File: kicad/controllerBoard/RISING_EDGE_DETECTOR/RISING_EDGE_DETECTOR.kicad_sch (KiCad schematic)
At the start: 17 parts, among them Q385 Q_PMOS_GSD, Q386 Q_NMOS_GSD, Q387 Q_PMOS_GSD, Q388 Q_NMOS_GSD, Q389 Q_PMOS_GSD, Q390 Q_NMOS_GSD, Q391 Q_PMOS_GSD, Q392 Q_NMOS_GSD

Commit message: add mounting holes
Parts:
- renumbered C3 to C1, C4 to C2, C5 to C3
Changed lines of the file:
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@@
 		(dnp no)
 		(fields_autoplaced yes)
-		(property "Reference" "#PWR090"
+		(property "Reference" "#PWR0138"
 			(at 120.65 80.01 0)
 			(hide yes)
@@
 			(project "controllerBoard"
 				(path "/93a9a1ca-4ee5-40da-ab67-92836146c003/96d1d3a9-3ebd-46ac-a2d2-b692fac1af2c"
-					(reference "#PWR090")
+					(reference "#PWR0138")
 					(unit 1)
 				)
 				(path "/93a9a1ca-4ee5-40da-ab67-92836146c003/def1fdf8-7002-45c6-87e0-28926b899265"
-					(reference "#PWR0122")
+					(reference "#PWR0204")
 					(unit 1)
 				)
@@
 		(dnp no)
 		(fields_autoplaced yes)
-		(property "Reference" "#PWR093"
+		(property "Reference" "#PWR0141"
 			(at 173.99 86.36 0)
 			(hide yes)
@@
 			(project "controllerBoard"
 				(path "/93a9a1ca-4ee5-40da-ab67-92836146c003/96d1d3a9-3ebd-46ac-a2d2-b692fac1af2c"
-					(reference "#PWR093")
+					(reference "#PWR0141")
 					(unit 1)
 				)
 				(path "/93a9a1ca-4ee5-40da-ab67-92836146c003/def1fdf8-7002-45c6-87e0-28926b899265"
-					(reference "#PWR0125")
+					(reference "#PWR0207")
 					(unit 1)
 				)
@@
 		(dnp no)
 		(fields_autoplaced yes)
-		(property "Reference" "#PWR088"
+		(property "Reference" "#PWR0136"
 			(at 99.06 52.07 0)
 			(hide yes)
@@
 			(project "controllerBoard"
 				(path "/93a9a1ca-4ee5-40da-ab67-92836146c003/96d1d3a9-3ebd-46ac-a2d2-b692fac1af2c"
-					(reference "#PWR088")
+					(reference "#PWR0136")
 					(unit 1)
 				)
 				(path "/93a9a1ca-4ee5-40da-ab67-92836146c003/def1fdf8-7002-45c6-87e0-28926b899265"
-					(reference "#PWR0120")
+					(reference "#PWR0202")
 					(unit 1)
 				)
@@
 		(dnp no)
 		(fields_autoplaced yes)
-		(property "Reference" "#PWR092"
+		(property "Reference" "#PWR0140"
 			(at 157.48 82.55 0)
 			(hide yes)
@@
 			(project "controllerBoard"
 				(path "/93a9a1ca-4ee5-40da-ab67-92836146c003/96d1d3a9-3ebd-46ac-a2d2-b692fac1af2c"
-					(reference "#PWR092")
+					(reference "#PWR0140")
 					(unit 1)
 				)
 				(path "/93a9a1ca-4ee5-40da-ab67-92836146c003/def1fdf8-7002-45c6-87e0-28926b899265"
-					(reference "#PWR0124")
+					(reference "#PWR0206")
 					(unit 1)
 				)
@@
 		(dnp no)
 		(fields_autoplaced yes)
-		(property "Reference" "#PWR094"
+		(property "Reference" "#PWR0142"
 			(at 201.93 62.23 0)
 			(hide yes)
@@
 			(project "controllerBoard"
 				(path "/93a9a1ca-4ee5-40da-ab67-92836146c003/96d1d3a9-3ebd-46ac-a2d2-b692fac1af2c"
-					(reference "#PWR094")
+					(reference "#PWR0142")
 					(unit 1)
 				)
 				(path "/93a9a1ca-4ee5-40da-ab67-92836146c003/def1fdf8-7002-45c6-87e0-28926b899265"
-					(reference "#PWR0126")
+					(reference "#PWR0208")
 					(unit 1)
 				)
@@
 		(dnp no)
 		(fields_autoplaced yes)
-		(property "Reference" "C3"
+		(property "Reference" "C1"
 			(at 107.95 58.42 90)
 			(show_name no)
@@
 			(project "controllerBoard"
 				(path "/93a9a1ca-4ee5-40da-ab67-92836146c003/96d1d3a9-3ebd-46ac-a2d2-b692fac1af2c"
-					(reference "C3")
+					(reference "C1")
 					(unit 1)
 				)
 				(path "/93a9a1ca-4ee5-40da-ab67-92836146c003/def1fdf8-7002-45c6-87e0-28926b899265"
-					(reference "C14")
+					(reference "C12")
 					(unit 1)
 				)
@@
 		(dnp no)
 		(fields_autoplaced yes)
-		(property "Reference" "C4"
+		(property "Reference" "C2"
 			(at 198.12 50.7999 0)
 			(show_name no)
@@
 			(project "controllerBoard"
 				(path "/93a9a1ca-4ee5-40da-ab67-92836146c003/96d1d3a9-3ebd-46ac-a2d2-b692fac1af2c"
-					(reference "C4")
+					(reference "C2")
 					(unit 1)
 				)
 				(path "/93a9a1ca-4ee5-40da-ab67-92836146c003/def1fdf8-7002-45c6-87e0-28926b899265"
-					(reference "C15")
+					(reference "C13")
 					(unit 1)
 				)
@@
 		(dnp no)
 		(fields_autoplaced yes)
-		(property "Reference" "#PWR087"
+		(property "Reference" "#PWR0135"
 			(at 88.9 82.55 0)
 			(hide yes)
@@
 			(project "controllerBoard"
 				(path "/93a9a1ca-4ee5-40da-ab67-92836146c003/96d1d3a9-3ebd-46ac-a2d2-b692fac1af2c"
-					(reference "#PWR087")
+					(reference "#PWR0135")
 					(unit 1)
 				)
 				(path "/93a9a1ca-4ee5-40da-ab67-92836146c003/def1fdf8-7002-45c6-87e0-28926b899265"
-					(reference "#PWR0119")
+					(reference "#PWR0201")
 					(unit 1)
 				)
@@
 		(dnp no)
 		(fields_autoplaced yes)
-		(property "Reference" "#PWR089"
+		(property "Reference" "#PWR0137"
 			(at 111.76 80.01 0)
 			(hide yes)
@@
 			(project "controllerBoard"
 				(path "/93a9a1ca-4ee5-40da-ab67-92836146c003/96d1d3a9-3ebd-46ac-a2d2-b692fac1af2c"
-					(reference "#PWR089")
+					(reference "#PWR0137")
 					(unit 1)
 				)
 				(path "/93a9a1ca-4ee5-40da-ab67-92836146c003/def1fdf8-7002-45c6-87e0-28926b899265"
-					(reference "#PWR0121")
+					(reference "#PWR0203")
 					(unit 1)
 				)
@@
 		(dnp no)
 		(fields_autoplaced yes)
-		(property "Reference" "C5"
+		(property "Reference" "C3"
 			(at 212.09 50.7999 0)
 			(show_name no)
@@
 			(project "controllerBoard"
 				(path "/93a9a1ca-4ee5-40da-ab67-92836146c003/96d1d3a9-3ebd-46ac-a2d2-b692fac1af2c"
-					(reference "C5")
+					(reference "C3")
 					(unit 1)
 				)
 				(path "/93a9a1ca-4ee5-40da-ab67-92836146c003/def1fdf8-7002-45c6-87e0-28926b899265"
-					(reference "C16")
+					(reference "C14")
 					(unit 1)
 				)
@@
 		(dnp no)
 		(fields_autoplaced yes)
-		(property "Reference" "#PWR091"
+		(property "Reference" "#PWR0139"
 			(at 137.16 82.55 0)
 			(hide yes)
@@
 			(project "controllerBoard"
 				(path "/93a9a1ca-4ee5-40da-ab67-92836146c003/96d1d3a9-3ebd-46ac-a2d2-b692fac1af2c"
-					(reference "#PWR091")
+					(reference "#PWR0139")
 					(unit 1)
 				)
 				(path "/93a9a1ca-4ee5-40da-ab67-92836146c003/def1fdf8-7002-45c6-87e0-28926b899265"
-					(reference "#PWR0123")
-					(unit 1)
-				)
+					(reference "#PWR0205")
+					(unit 1)
+				)

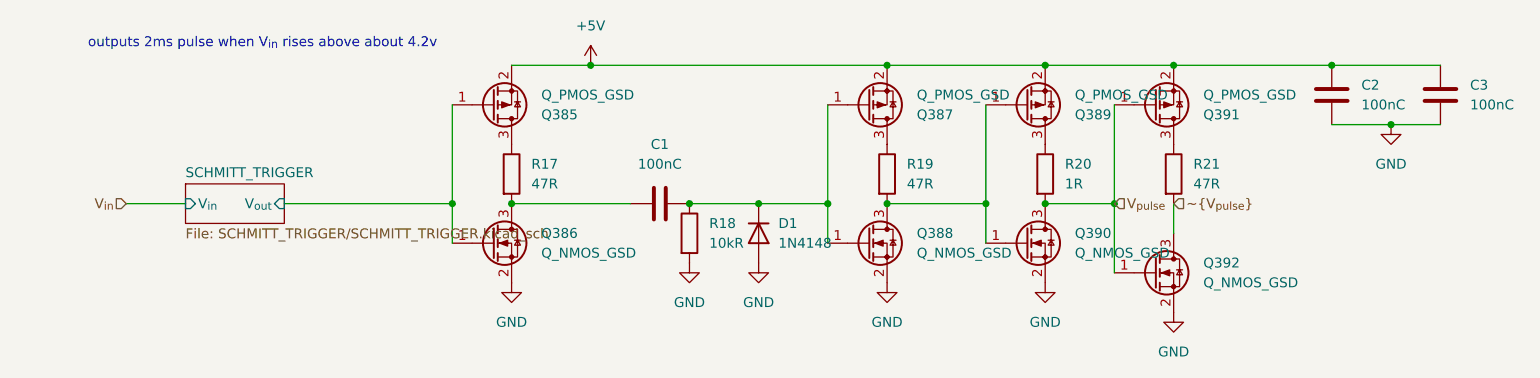
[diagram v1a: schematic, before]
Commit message: update bom, add more capacitors
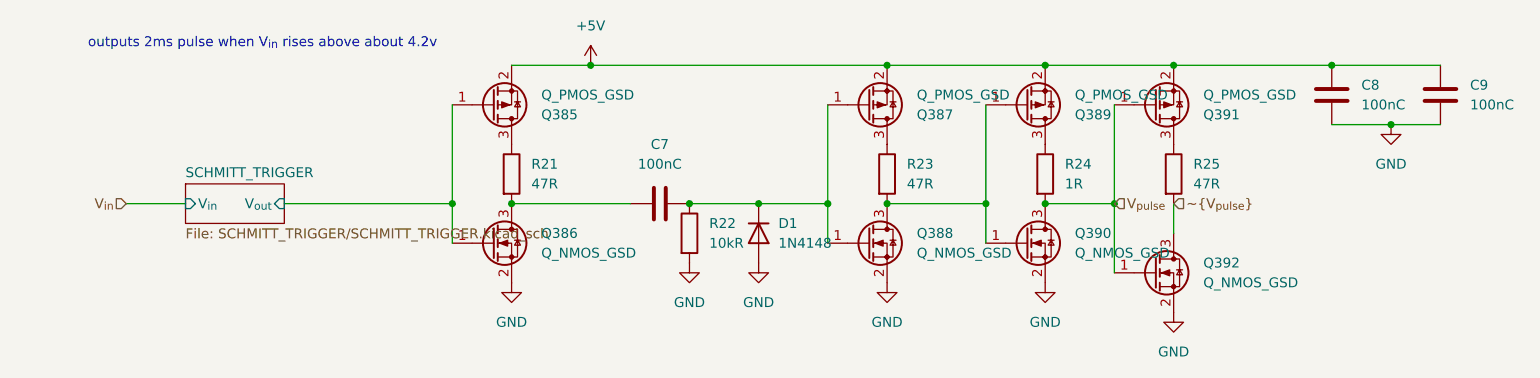
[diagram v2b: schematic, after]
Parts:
- renumbered C1 to C7, C2 to C8, C3 to C9, R17 to R21, R18 to R22, R19 to R23, R20 to R24, R21 to R25
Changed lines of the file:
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@@
 		(dnp no)
 		(fields_autoplaced yes)
-		(property "Reference" "#PWR0138"
+		(property "Reference" "#PWR0145"
 			(at 120.65 80.01 0)
 			(hide yes)
@@
 			(project "controllerBoard"
 				(path "/93a9a1ca-4ee5-40da-ab67-92836146c003/96d1d3a9-3ebd-46ac-a2d2-b692fac1af2c"
-					(reference "#PWR0138")
+					(reference "#PWR0145")
 					(unit 1)
 				)
 				(path "/93a9a1ca-4ee5-40da-ab67-92836146c003/def1fdf8-7002-45c6-87e0-28926b899265"
-					(reference "#PWR0204")
+					(reference "#PWR0211")
 					(unit 1)
 				)
@@
 		(dnp no)
 		(fields_autoplaced yes)
-		(property "Reference" "#PWR0141"
+		(property "Reference" "#PWR0148"
 			(at 173.99 86.36 0)
 			(hide yes)
@@
 			(project "controllerBoard"
 				(path "/93a9a1ca-4ee5-40da-ab67-92836146c003/96d1d3a9-3ebd-46ac-a2d2-b692fac1af2c"
-					(reference "#PWR0141")
+					(reference "#PWR0148")
 					(unit 1)
 				)
 				(path "/93a9a1ca-4ee5-40da-ab67-92836146c003/def1fdf8-7002-45c6-87e0-28926b899265"
-					(reference "#PWR0207")
+					(reference "#PWR0214")
 					(unit 1)
 				)
@@
 		(dnp no)
 		(fields_autoplaced yes)
-		(property "Reference" "R17"
+		(property "Reference" "R21"
 			(at 91.44 60.9599 0)
 			(show_name no)
@@
 			(project "controllerBoard"
 				(path "/93a9a1ca-4ee5-40da-ab67-92836146c003/96d1d3a9-3ebd-46ac-a2d2-b692fac1af2c"
-					(reference "R17")
+					(reference "R21")
 					(unit 1)
 				)
 				(path "/93a9a1ca-4ee5-40da-ab67-92836146c003/def1fdf8-7002-45c6-87e0-28926b899265"
-					(reference "R34")
+					(reference "R38")
 					(unit 1)
 				)
@@
 		(dnp no)
 		(fields_autoplaced yes)
-		(property "Reference" "#PWR0136"
+		(property "Reference" "#PWR0143"
 			(at 99.06 52.07 0)
 			(hide yes)
@@
 			(project "controllerBoard"
 				(path "/93a9a1ca-4ee5-40da-ab67-92836146c003/96d1d3a9-3ebd-46ac-a2d2-b692fac1af2c"
-					(reference "#PWR0136")
+					(reference "#PWR0143")
 					(unit 1)
 				)
 				(path "/93a9a1ca-4ee5-40da-ab67-92836146c003/def1fdf8-7002-45c6-87e0-28926b899265"
-					(reference "#PWR0202")
+					(reference "#PWR0209")
 					(unit 1)
 				)
@@
 		(dnp no)
 		(fields_autoplaced yes)
-		(property "Reference" "#PWR0140"
+		(property "Reference" "#PWR0147"
 			(at 157.48 82.55 0)
 			(hide yes)
@@
 			(project "controllerBoard"
 				(path "/93a9a1ca-4ee5-40da-ab67-92836146c003/96d1d3a9-3ebd-46ac-a2d2-b692fac1af2c"
-					(reference "#PWR0140")
+					(reference "#PWR0147")
 					(unit 1)
 				)
 				(path "/93a9a1ca-4ee5-40da-ab67-92836146c003/def1fdf8-7002-45c6-87e0-28926b899265"
-					(reference "#PWR0206")
+					(reference "#PWR0213")
 					(unit 1)
 				)
@@
 		(dnp no)
 		(fields_autoplaced yes)
-		(property "Reference" "#PWR0142"
+		(property "Reference" "#PWR0149"
 			(at 201.93 62.23 0)
 			(hide yes)
@@
 			(project "controllerBoard"
 				(path "/93a9a1ca-4ee5-40da-ab67-92836146c003/96d1d3a9-3ebd-46ac-a2d2-b692fac1af2c"
-					(reference "#PWR0142")
+					(reference "#PWR0149")
 					(unit 1)
 				)
 				(path "/93a9a1ca-4ee5-40da-ab67-92836146c003/def1fdf8-7002-45c6-87e0-28926b899265"
-					(reference "#PWR0208")
+					(reference "#PWR0215")
 					(unit 1)
 				)
@@
 		(dnp no)
 		(fields_autoplaced yes)
-		(property "Reference" "C1"
+		(property "Reference" "C7"
 			(at 107.95 58.42 90)
 			(show_name no)
@@
 			(project "controllerBoard"
 				(path "/93a9a1ca-4ee5-40da-ab67-92836146c003/96d1d3a9-3ebd-46ac-a2d2-b692fac1af2c"
-					(reference "C1")
+					(reference "C7")
 					(unit 1)
 				)
 				(path "/93a9a1ca-4ee5-40da-ab67-92836146c003/def1fdf8-7002-45c6-87e0-28926b899265"
-					(reference "C12")
+					(reference "C18")
 					(unit 1)
 				)
@@
 		(dnp no)
 		(fields_autoplaced yes)
-		(property "Reference" "C2"
+		(property "Reference" "C8"
 			(at 198.12 50.7999 0)
 			(show_name no)
@@
 			(project "controllerBoard"
 				(path "/93a9a1ca-4ee5-40da-ab67-92836146c003/96d1d3a9-3ebd-46ac-a2d2-b692fac1af2c"
-					(reference "C2")
+					(reference "C8")
 					(unit 1)
 				)
 				(path "/93a9a1ca-4ee5-40da-ab67-92836146c003/def1fdf8-7002-45c6-87e0-28926b899265"
-					(reference "C13")
+					(reference "C19")
 					(unit 1)
 				)
@@
 		(dnp no)
 		(fields_autoplaced yes)
-		(property "Reference" "#PWR0135"
+		(property "Reference" "#PWR0142"
 			(at 88.9 82.55 0)
 			(hide yes)
@@
 			(project "controllerBoard"
 				(path "/93a9a1ca-4ee5-40da-ab67-92836146c003/96d1d3a9-3ebd-46ac-a2d2-b692fac1af2c"
-					(reference "#PWR0135")
+					(reference "#PWR0142")
 					(unit 1)
 				)
 				(path "/93a9a1ca-4ee5-40da-ab67-92836146c003/def1fdf8-7002-45c6-87e0-28926b899265"
-					(reference "#PWR0201")
+					(reference "#PWR0208")
 					(unit 1)
 				)
@@
 		(dnp no)
 		(fields_autoplaced yes)
-		(property "Reference" "R20"
+		(property "Reference" "R24"
 			(at 160.02 60.9599 0)
 			(show_name no)
@@
 			(project "controllerBoard"
 				(path "/93a9a1ca-4ee5-40da-ab67-92836146c003/96d1d3a9-3ebd-46ac-a2d2-b692fac1af2c"
-					(reference "R20")
+					(reference "R24")
 					(unit 1)
 				)
 				(path "/93a9a1ca-4ee5-40da-ab67-92836146c003/def1fdf8-7002-45c6-87e0-28926b899265"
-					(reference "R37")
+					(reference "R41")
 					(unit 1)
 				)
@@
 		(dnp no)
 		(fields_autoplaced yes)
-		(property "Reference" "R18"
+		(property "Reference" "R22"
 			(at 114.3 68.5799 0)
 			(show_name no)
@@
 			(project "controllerBoard"
 				(path "/93a9a1ca-4ee5-40da-ab67-92836146c003/96d1d3a9-3ebd-46ac-a2d2-b692fac1af2c"
-					(reference "R18")
+					(reference "R22")
 					(unit 1)
 				)
 				(path "/93a9a1ca-4ee5-40da-ab67-92836146c003/def1fdf8-7002-45c6-87e0-28926b899265"
-					(reference "R35")
+					(reference "R39")
 					(unit 1)
 				)
@@
 		(dnp no)
 		(fields_autoplaced yes)
-		(property "Reference" "R19"
+		(property "Reference" "R23"
 			(at 139.7 60.9599 0)
 			(show_name no)
@@
 			(project "controllerBoard"
 				(path "/93a9a1ca-4ee5-40da-ab67-92836146c003/96d1d3a9-3ebd-46ac-a2d2-b692fac1af2c"
-					(reference "R19")
+					(reference "R23")
 					(unit 1)
 				)
 				(path "/93a9a1ca-4ee5-40da-ab67-92836146c003/def1fdf8-7002-45c6-87e0-28926b899265"
-					(reference "R36")
+					(reference "R40")
 					(unit 1)
 				)
@@
 		(dnp no)
 		(fields_autoplaced yes)
-		(property "Reference" "#PWR0137"
+		(property "Reference" "#PWR0144"
 			(at 111.76 80.01 0)
 			(hide yes)
@@
 			(project "controllerBoard"
 				(path "/93a9a1ca-4ee5-40da-ab67-92836146c003/96d1d3a9-3ebd-46ac-a2d2-b692fac1af2c"
-					(reference "#PWR0137")
+					(reference "#PWR0144")
 					(unit 1)
 				)
 				(path "/93a9a1ca-4ee5-40da-ab67-92836146c003/def1fdf8-7002-45c6-87e0-28926b899265"
-					(reference "#PWR0203")
+					(reference "#PWR0210")
 					(unit 1)
 				)
@@
 		(dnp no)
 		(fields_autoplaced yes)
-		(property "Reference" "R21"
+		(property "Reference" "R25"
 			(at 176.53 60.9599 0)
 			(show_name no)
@@
 			(project "controllerBoard"
 				(path "/93a9a1ca-4ee5-40da-ab67-92836146c003/96d1d3a9-3ebd-46ac-a2d2-b692fac1af2c"
-					(reference "R21")
+					(reference "R25")
 					(unit 1)
 				)
 				(path "/93a9a1ca-4ee5-40da-ab67-92836146c003/def1fdf8-7002-45c6-87e0-28926b899265"
-					(reference "R38")
+					(reference "R42")
 					(unit 1)
 				)
@@
 		(dnp no)
 		(fields_autoplaced yes)
-		(property "Reference" "C3"
+		(property "Reference" "C9"
 			(at 212.09 50.7999 0)
 			(show_name no)
@@
 			(project "controllerBoard"
 				(path "/93a9a1ca-4ee5-40da-ab67-92836146c003/96d1d3a9-3ebd-46ac-a2d2-b692fac1af2c"
-					(reference "C3")
+					(reference "C9")
 					(unit 1)
 				)
 				(path "/93a9a1ca-4ee5-40da-ab67-92836146c003/def1fdf8-7002-45c6-87e0-28926b899265"
-					(reference "C14")
+					(reference "C20")
 					(unit 1)
 				)
@@
 		(dnp no)
 		(fields_autoplaced yes)
-		(property "Reference" "#PWR0139"
+		(property "Reference" "#PWR0146"
 			(at 137.16 82.55 0)
 			(hide yes)
@@
 			(project "controllerBoard"
 				(path "/93a9a1ca-4ee5-40da-ab67-92836146c003/96d1d3a9-3ebd-46ac-a2d2-b692fac1af2c"
-					(reference "#PWR0139")
+					(reference "#PWR0146")
 					(unit 1)
 				)
 				(path "/93a9a1ca-4ee5-40da-ab67-92836146c003/def1fdf8-7002-45c6-87e0-28926b899265"
-					(reference "#PWR0205")
-					(unit 1)
-				)
+					(reference "#PWR0212")
+					(unit 1)
+				)
